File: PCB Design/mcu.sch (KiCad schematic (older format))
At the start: 11 parts, among them P14 ICSP, U4 dsPIC33FJ32GS606, X2 10MHz

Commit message: PCB is now 10cmx5cm, some components moved around for more space
Signed-off-by: Kolijn Wolfaardt <kolijn.wolfaardt@gmail.com>
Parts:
- P16: renamed from P?; footprint (none) -> Pin_Headers:Pin_Header_Straight_1x03
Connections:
- wire segments 115 -> 107
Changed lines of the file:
@@
 $EndComp
 $Comp
-L +3V3 #PWR053
+L +3V3 #PWR055
 U 1 1 550F44AC
 P 2400 6150
-F 0 "#PWR053" H 2400 6000 60  0001 C CNN
+F 0 "#PWR055" H 2400 6000 60  0001 C CNN
 F 1 "+3V3" H 2400 6290 60  0000 C CNN
 F 2 "" H 2400 6150 60  0000 C CNN
@@
 $EndComp
 $Comp
-L GND #PWR054
+L GND #PWR056
 U 1 1 550F44B3
 P 2400 6450
-F 0 "#PWR054" H 2400 6200 60  0001 C CNN
+F 0 "#PWR056" H 2400 6200 60  0001 C CNN
 F 1 "GND" H 2400 6300 60  0000 C CNN
 F 2 "" H 2400 6450 60  0000 C CNN
@@
 MCLR_in
 $Comp
-L +3V3 #PWR055
+L +3V3 #PWR057
 U 1 1 550F44C2
 P 2250 3700
-F 0 "#PWR055" H 2250 3550 60  0001 C CNN
+F 0 "#PWR057" H 2250 3550 60  0001 C CNN
 F 1 "+3V3" H 2250 3840 60  0000 C CNN
 F 2 "" H 2250 3700 60  0000 C CNN
@@
 $EndComp
 $Comp
-L GND #PWR056
+L GND #PWR058
 U 1 1 550F44C8
 P 2000 4350
-F 0 "#PWR056" H 2000 4100 60  0001 C CNN
+F 0 "#PWR058" H 2000 4100 60  0001 C CNN
 F 1 "GND" H 2000 4200 60  0000 C CNN
 F 2 "" H 2000 4350 60  0000 C CNN
@@
 $EndComp
 $Comp
-L +3V3 #PWR057
+L +3V3 #PWR059
 U 1 1 550F44D2
 P 2200 2000
-F 0 "#PWR057" H 2200 1850 60  0001 C CNN
+F 0 "#PWR059" H 2200 1850 60  0001 C CNN
 F 1 "+3V3" H 2200 2140 60  0000 C CNN
 F 2 "" H 2200 2000 60  0000 C CNN
@@
 $EndComp
 $Comp
-L GND #PWR058
+L GND #PWR060
 U 1 1 550F44D8
 P 2000 2650
-F 0 "#PWR058" H 2000 2400 60  0001 C CNN
+F 0 "#PWR060" H 2000 2400 60  0001 C CNN
 F 1 "GND" H 2000 2500 60  0000 C CNN
 F 2 "" H 2000 2650 60  0000 C CNN
@@
 $EndComp
 $Comp
-L +3V3 #PWR059
+L +3V3 #PWR061
 U 1 1 550F44E2
 P 8000 3950
-F 0 "#PWR059" H 8000 3800 60  0001 C CNN
+F 0 "#PWR061" H 8000 3800 60  0001 C CNN
 F 1 "+3V3" H 8000 4090 60  0000 C CNN
 F 2 "" H 8000 3950 60  0000 C CNN
@@
 $EndComp
 $Comp
-L GND #PWR060
+L GND #PWR062
 U 1 1 550F44E8
 P 7800 3700
-F 0 "#PWR060" H 7800 3450 60  0001 C CNN
+F 0 "#PWR062" H 7800 3450 60  0001 C CNN
 F 1 "GND" H 7800 3550 60  0000 C CNN
 F 2 "" H 7800 3700 60  0000 C CNN
@@
 $EndComp
 $Comp
-L +3V3 #PWR061
+L +3V3 #PWR063
 U 1 1 550F44F1
 P 7850 1900
-F 0 "#PWR061" H 7850 1750 60  0001 C CNN
+F 0 "#PWR063" H 7850 1750 60  0001 C CNN
 F 1 "+3V3" H 7850 2040 60  0000 C CNN
 F 2 "" H 7850 1900 60  0000 C CNN
@@
 PGC
 $Comp
-L +3V3 #PWR062
+L +3V3 #PWR064
 U 1 1 550F450D
 P 2100 3100
-F 0 "#PWR062" H 2100 2950 60  0001 C CNN
+F 0 "#PWR064" H 2100 2950 60  0001 C CNN
 F 1 "+3V3" H 2100 3240 60  0000 C CNN
 F 2 "" H 2100 3100 60  0000 C CNN
@@
 $EndComp
 $Comp
-L GND #PWR063
+L GND #PWR065
 U 1 1 550F4513
 P 2100 3350
-F 0 "#PWR063" H 2100 3100 60  0001 C CNN
+F 0 "#PWR065" H 2100 3100 60  0001 C CNN
 F 1 "GND" H 2100 3200 60  0000 C CNN
 F 2 "" H 2100 3350 60  0000 C CNN
@@
 $EndComp
 $Comp
-L GND #PWR064
+L GND #PWR066
 U 1 1 550F453B
 P 4550 6600
-F 0 "#PWR064" H 4550 6350 60  0001 C CNN
+F 0 "#PWR066" H 4550 6350 60  0001 C CNN
 F 1 "GND" H 4550 6450 60  0000 C CNN
 F 2 "" H 4550 6600 60  0000 C CNN
@@
 $EndComp
 $Comp
-L GND #PWR065
+L GND #PWR067
 U 1 1 550F4558
 P 6100 6700
-F 0 "#PWR065" H 6100 6450 60  0001 C CNN
+F 0 "#PWR067" H 6100 6450 60  0001 C CNN
 F 1 "GND" H 6100 6550 60  0000 C CNN
 F 2 "" H 6100 6700 60  0000 C CNN
@@
 Vcap
 $Comp
-L +3V3 #PWR066
+L +3V3 #PWR068
 U 1 1 550F4674
 P 9100 5650
-F 0 "#PWR066" H 9100 5500 60  0001 C CNN
+F 0 "#PWR068" H 9100 5500 60  0001 C CNN
 F 1 "+3V3" H 9100 5790 60  0000 C CNN
 F 2 "" H 9100 5650 60  0000 C CNN
@@
 $EndComp
 $Comp
-L GND #PWR067
+L GND #PWR069
 U 1 1 550F46C2
 P 9100 5800
-F 0 "#PWR067" H 9100 5550 60  0001 C CNN
+F 0 "#PWR069" H 9100 5550 60  0001 C CNN
 F 1 "GND" H 9100 5650 60  0000 C CNN
 F 2 "" H 9100 5800 60  0000 C CNN
@@
 $EndComp
 $Comp
-L GND #PWR068
+L GND #PWR070
 U 1 1 551050BF
 P 9900 3650
-F 0 "#PWR068" H 9900 3400 60  0001 C CNN
+F 0 "#PWR070" H 9900 3400 60  0001 C CNN
 F 1 "GND" H 9900 3500 60  0000 C CNN
 F 2 "" H 9900 3650 60  0000 C CNN
@@
 MCLR_in
 $Comp
-L +3V3 #PWR069
+L +3V3 #PWR071
 U 1 1 5510573C
 P 9700 1750
-F 0 "#PWR069" H 9700 1600 60  0001 C CNN
+F 0 "#PWR071" H 9700 1600 60  0001 C CNN
 F 1 "+3V3" H 9700 1890 60  0000 C CNN
 F 2 "" H 9700 1750 60  0000 C CNN
@@
 $EndComp
 $Comp
-L GND #PWR070
+L GND #PWR072
 U 1 1 55105A71
 P 9350 3050
-F 0 "#PWR070" H 9350 2800 60  0001 C CNN
+F 0 "#PWR072" H 9350 2800 60  0001 C CNN
 F 1 "GND" H 9350 2900 60  0000 C CNN
 F 2 "" H 9350 3050 60  0000 C CNN
@@
 	2950 1900 3400 1900
 Wire Wire Line
-	4550 5900 4550 6500
-Wire Wire Line
-	4550 6500 4550 6600
+	4550 5900 4550 6600
 Wire Wire Line
 	4400 5900 4550 5900
@@
 	3950 6400 3950 6500
 Wire Wire Line
-	3350 6500 3950 6500
-Wire Wire Line
-	3950 6500 4100 6500
+	3350 6500 4100 6500
 Connection ~ 3950 6500
 Wire Wire Line
-	3350 5900 3950 5900
-Wire Wire Line
-	3950 5900 4100 5900
+	3350 5900 4100 5900
 Wire Wire Line
 	3950 6000 3950 5900
@@
 	9700 3550 9700 3650
 Wire Wire Line
-	9700 3650 9900 3650
-Wire Wire Line
-	9900 3650 10100 3650
+	9700 3650 10100 3650
 Wire Wire Line
 	10100 3650 10100 3550
 Connection ~ 9900 3650
 Wire Wire Line
-	9100 2450 9350 2450
-Wire Wire Line
-	9350 2450 9700 2450
-Wire Wire Line
-	9700 2450 10100 2450
-Wire Wire Line
-	10100 2450 10600 2450
-Wire Wire Line
-	9700 2250 9700 2450
-Wire Wire Line
-	9700 2450 9700 2550
+	9100 2450 10600 2450
+Wire Wire Line
+	9700 2250 9700 2550
 Connection ~ 9700 2450
 Wire Wire Line
@@
 	3550 6200 3550 6250
 $Comp
-L GND #PWR071
+L GND #PWR073
 U 1 1 5513A6E9
 P 3550 6250
-F 0 "#PWR071" H 3550 6000 60  0001 C CNN
+F 0 "#PWR073" H 3550 6000 60  0001 C CNN
 F 1 "GND" H 3550 6100 60  0000 C CNN
 F 2 "" H 3550 6250 60  0000 C CNN
@@
 NoConn ~ 7150 1900
 $Comp
-L CONN_01X03 P?
+L CONN_01X03 P16
 U 1 1 551D06D3
 P 9700 4650
-F 0 "P?" H 9700 4850 50  0000 C CNN
+F 0 "P16" H 9700 4850 50  0000 C CNN
 F 1 "UART" V 9800 4650 50  0000 C CNN
-F 2 "" H 9700 4650 60  0000 C CNN
+F 2 "Pin_Headers:Pin_Header_Straight_1x03" H 9700 4650 60  0001 C CNN
 F 3 "" H 9700 4650 60  0000 C CNN
 	1    9700 4650
@@
 U1TX
 $Comp
-L GND #PWR?
+L GND #PWR074
 U 1 1 551D07D4
 P 8950 4700
-F 0 "#PWR?" H 8950 4450 60  0001 C CNN
+F 0 "#PWR074" H 8950 4450 60  0001 C CNN
 F 1 "GND" H 8950 4550 60  0000 C CNN
 F 2 "" H 8950 4700 60  0000 C CNN

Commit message: Removed connection between data_4 and data_5
Signed-off-by: Kolijn_Laptop <kolijn.wolfaardt@gmail.com>
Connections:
- net labels removed: Data_5
- no-connect marks 3 -> 4
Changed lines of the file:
@@
 Text HLabel 7200 2300 2    60   Input ~ 0
 Data_6
-Text HLabel 7200 2400 2    60   Input ~ 0
-Data_5
 Text HLabel 7200 2500 2    60   Input ~ 0
 Data_4
@@
 Wire Wire Line
 	9400 4750 9500 4750
+NoConn ~ 7200 2400
 $EndSCHEMATC

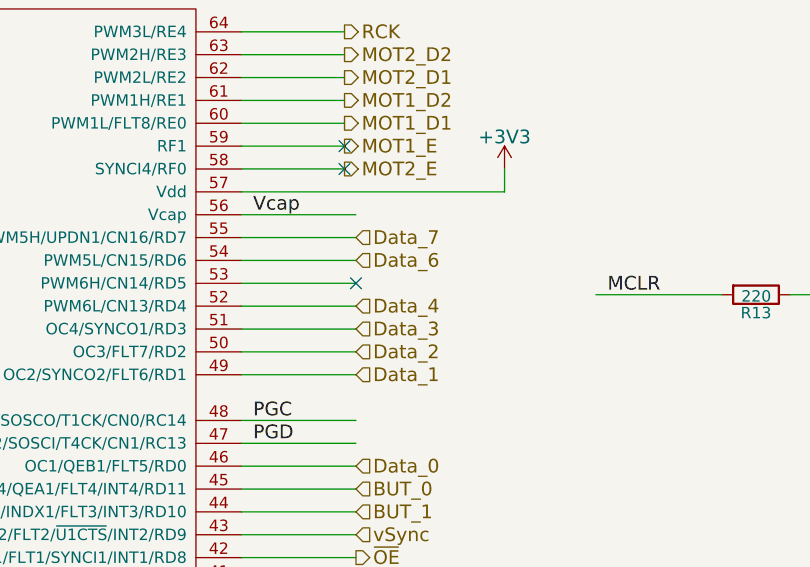
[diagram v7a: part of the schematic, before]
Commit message: Motor Diodes done, some of the power connections
Signed-off-by: Kolijn_Laptop <kolijn.wolfaardt@gmail.com>
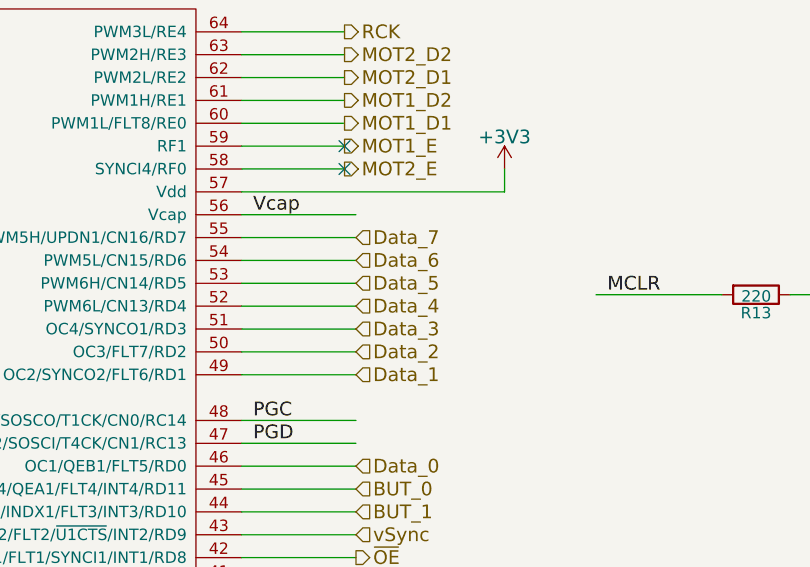
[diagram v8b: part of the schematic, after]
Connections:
- net labels added: Data_5
- no-connect marks 4 -> 3
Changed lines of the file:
@@
 Text HLabel 7200 2300 2    60   Input ~ 0
 Data_6
-Text HLabel 7200 2500 2    60   Input ~ 0
-Data_4
 Text HLabel 7200 2600 2    60   Input ~ 0
 Data_3
@@
 Wire Wire Line
 	9400 4750 9500 4750
-NoConn ~ 7200 2400
+Text HLabel 7200 2500 2    60   Input ~ 0
+Data_4
+Text HLabel 7200 2400 2    60   Input ~ 0
+Data_5
 $EndSCHEMATC
